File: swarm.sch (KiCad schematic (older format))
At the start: 24 parts, among them P1 USB_OTG, P2 CONN_02X20, P3 CONN_01X05, SW1 SW_PUSH, U1 STM32F103RETx, U2 LM3671MF-3.3, Y1 Crystal

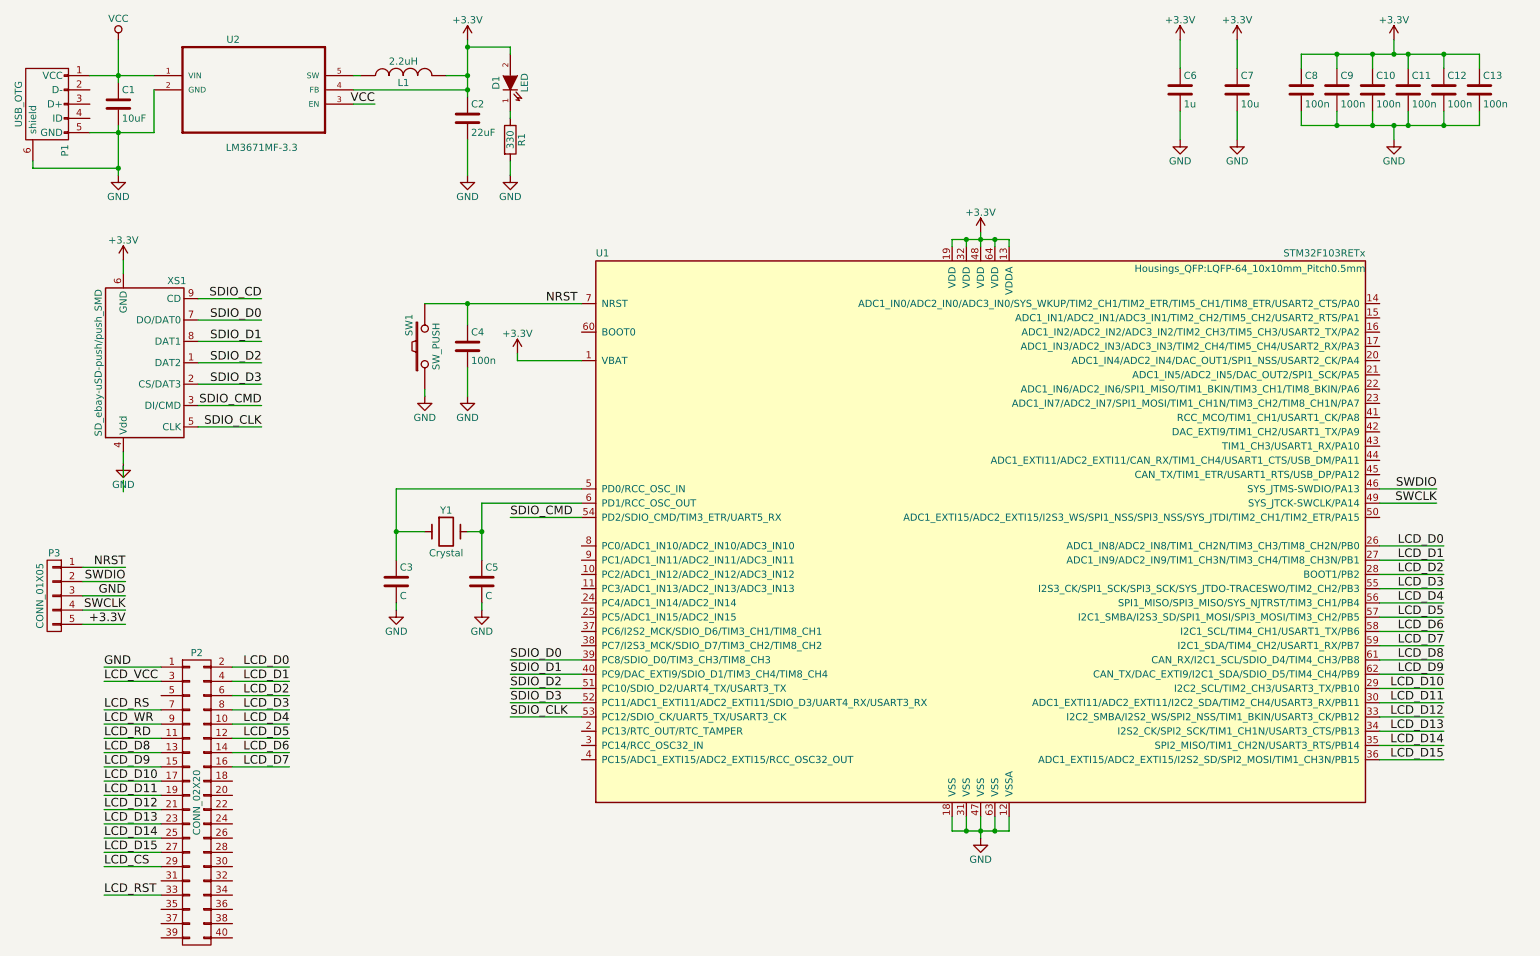
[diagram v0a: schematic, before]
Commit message: Adds APA102 SPI RGB LED Updates schematic references and links docoupling capacitors based on input pin
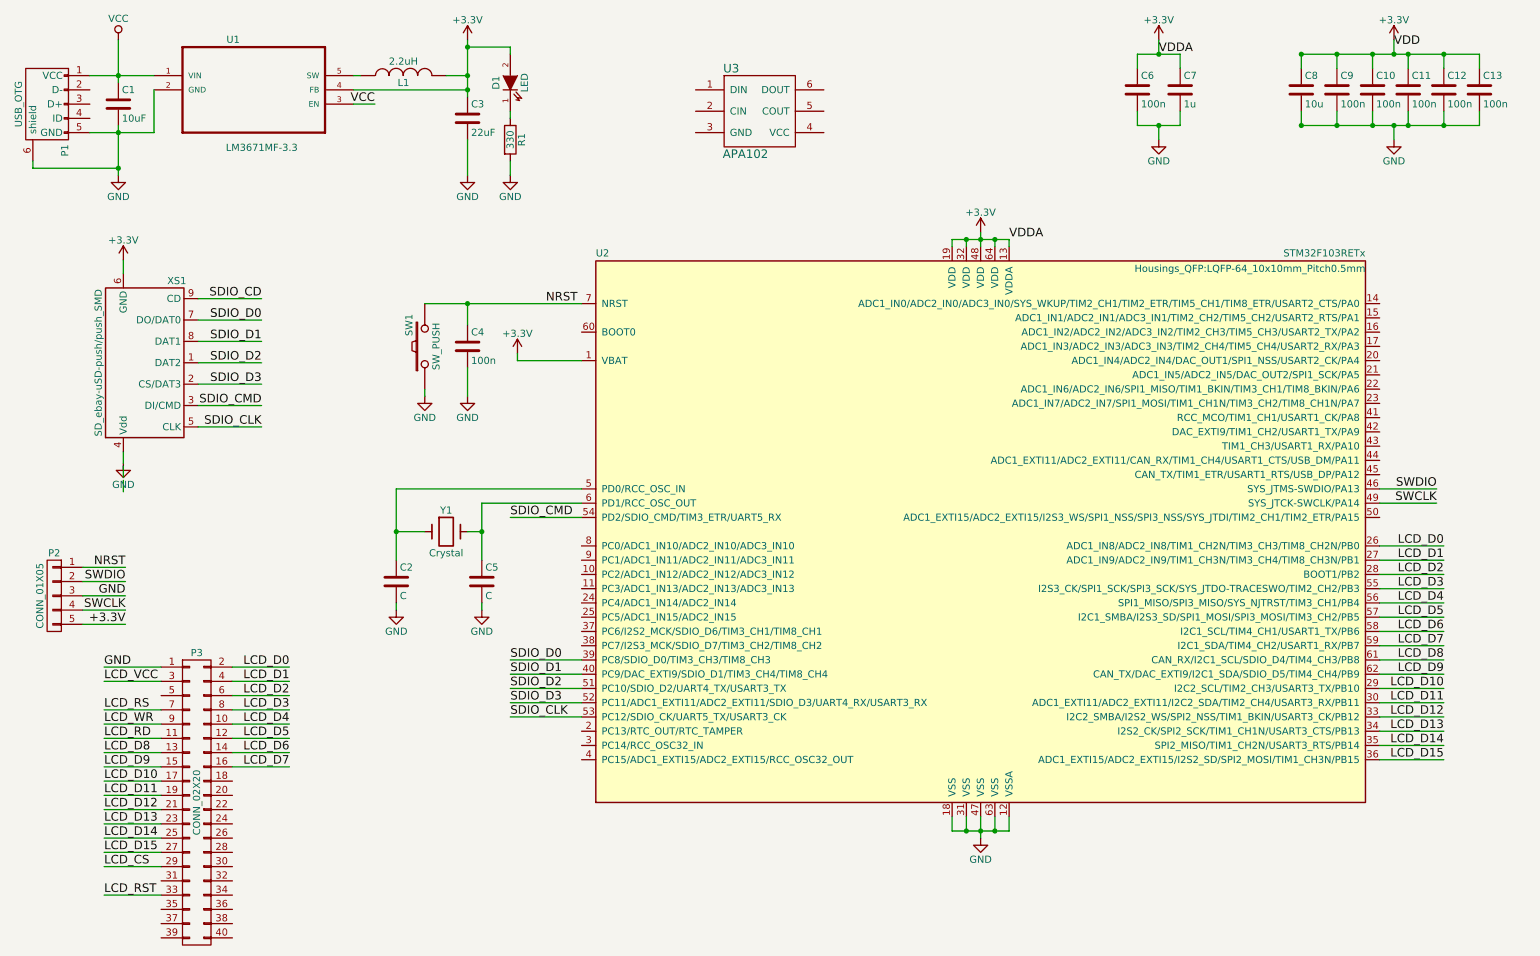
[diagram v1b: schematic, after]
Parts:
- added U3: APA102, volium:APA102, symbol APA102
- renumbered C3 to C2, C2 to C3, C8 to C6, C6 to C7, C7 to C8, P3 to P2, P2 to P3, U2 to U1, U1 to U2
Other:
- moved on the sheet: C6, C8
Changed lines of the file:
@@
 $EndDescr
 $Comp
-L +3.3V #PWR01
+L +3.3V #PWR13
 U 1 1 58134F73
 P 7450 2100
-F 0 "#PWR01" H 7450 1950 50  0001 C CNN
+F 0 "#PWR13" H 7450 1950 50  0001 C CNN
 F 1 "+3.3V" H 7450 2240 50  0000 C CNN
 F 2 "" H 7450 2100 50  0000 C CNN
@@
 $EndComp
 $Comp
-L GND #PWR02
+L GND #PWR14
 U 1 1 58134F89
 P 7450 6350
-F 0 "#PWR02" H 7450 6100 50  0001 C CNN
+F 0 "#PWR14" H 7450 6100 50  0001 C CNN
 F 1 "GND" H 7450 6200 50  0000 C CNN
 F 2 "" H 7450 6350 50  0000 C CNN
@@
 $EndComp
 $Comp
-L STM32F103RETx U1
+L STM32F103RETx U2
 U 1 1 581356E3
 P 7450 4200
-F 0 "U1" H 4750 6125 50  0000 L BNN
+F 0 "U2" H 4750 6125 50  0000 L BNN
 F 1 "STM32F103RETx" H 10150 6125 50  0000 R BNN
 F 2 "Housings_QFP:LQFP-64_10x10mm_Pitch0.5mm" H 10150 6075 50  0000 R TNN
@@
 $EndComp
 $Comp
-L +3.3V #PWR03
+L +3.3V #PWR12
 U 1 1 581369FC
 P 4200 2950
-F 0 "#PWR03" H 4200 2800 50  0001 C CNN
+F 0 "#PWR12" H 4200 2800 50  0001 C CNN
 F 1 "+3.3V" H 4200 3090 50  0000 C CNN
 F 2 "" H 4200 2950 50  0000 C CNN
@@
 $EndComp
 $Comp
-L C C8
+L C C6
 U 1 1 58136AF0
-P 9700 1100
-F 0 "C8" H 9725 1200 50  0000 L CNN
-F 1 "100n" H 9725 1000 50  0000 L CNN
-F 2 "Capacitors_SMD:C_1206" H 9738 950 50  0001 C CNN
-F 3 "" H 9700 1100 50  0000 C CNN
-	1    9700 1100
+P 8550 1100
+F 0 "C6" H 8575 1200 50  0000 L CNN
+F 1 "100n" H 8575 1000 50  0000 L CNN
+F 2 "Capacitors_SMD:C_1206" H 8588 950 50  0001 C CNN
+F 3 "" H 8550 1100 50  0000 C CNN
+	1    8550 1100
 	1    0    0    -1
 $EndComp
@@
 $EndComp
 $Comp
-L +3.3V #PWR04
+L +3.3V #PWR17
 U 1 1 58136B0C
 P 10350 750
-F 0 "#PWR04" H 10350 600 50  0001 C CNN
+F 0 "#PWR17" H 10350 600 50  0001 C CNN
 F 1 "+3.3V" H 10350 890 50  0000 C CNN
 F 2 "" H 10350 750 50  0000 C CNN
@@
 $EndComp
 $Comp
-L GND #PWR05
+L GND #PWR18
 U 1 1 58136D49
 P 10350 1450
-F 0 "#PWR05" H 10350 1200 50  0001 C CNN
+F 0 "#PWR18" H 10350 1200 50  0001 C CNN
 F 1 "GND" H 10350 1300 50  0000 C CNN
 F 2 "" H 10350 1450 50  0000 C CNN
@@
 $EndComp
 $Comp
+L C C8
+U 1 1 58137098
+P 9700 1100
+F 0 "C8" H 9725 1200 50  0000 L CNN
+F 1 "10u" H 9725 1000 50  0000 L CNN
+F 2 "Capacitors_SMD:C_1206" H 9738 950 50  0001 C CNN
+F 3 "" H 9700 1100 50  0000 C CNN
+	1    9700 1100
+	1    0    0    -1
+$EndComp
+$Comp
 L C C7
-U 1 1 58137098
-P 9250 1100
-F 0 "C7" H 9275 1200 50  0000 L CNN
-F 1 "10u" H 9275 1000 50  0000 L CNN
-F 2 "Capacitors_SMD:C_1206" H 9288 950 50  0001 C CNN
-F 3 "" H 9250 1100 50  0000 C CNN
-	1    9250 1100
-	1    0    0    -1
-$EndComp
-$Comp
-L +3.3V #PWR06
-U 1 1 581373B1
-P 9250 750
-F 0 "#PWR06" H 9250 600 50  0001 C CNN
-F 1 "+3.3V" H 9250 890 50  0000 C CNN
-F 2 "" H 9250 750 50  0000 C CNN
-F 3 "" H 9250 750 50  0000 C CNN
-	1    9250 750
-	1    0    0    -1
-$EndComp
-$Comp
-L GND #PWR07
-U 1 1 581375CE
-P 9250 1450
-F 0 "#PWR07" H 9250 1200 50  0001 C CNN
-F 1 "GND" H 9250 1300 50  0000 C CNN
-F 2 "" H 9250 1450 50  0000 C CNN
-F 3 "" H 9250 1450 50  0000 C CNN
-	1    9250 1450
-	1    0    0    -1
-$EndComp
-$Comp
-L C C6
 U 1 1 581377A0
 P 8850 1100
-F 0 "C6" H 8875 1200 50  0000 L CNN
+F 0 "C7" H 8875 1200 50  0000 L CNN
 F 1 "1u" H 8875 1000 50  0000 L CNN
 F 2 "Capacitors_SMD:C_1206" H 8888 950 50  0001 C CNN
@@
 $EndComp
 $Comp
-L +3.3V #PWR08
+L +3.3V #PWR15
 U 1 1 581377EE
-P 8850 750
-F 0 "#PWR08" H 8850 600 50  0001 C CNN
-F 1 "+3.3V" H 8850 890 50  0000 C CNN
-F 2 "" H 8850 750 50  0000 C CNN
-F 3 "" H 8850 750 50  0000 C CNN
-	1    8850 750
-	1    0    0    -1
-$EndComp
-$Comp
-L GND #PWR09
+P 8700 750
+F 0 "#PWR15" H 8700 600 50  0001 C CNN
+F 1 "+3.3V" H 8700 890 50  0000 C CNN
+F 2 "" H 8700 750 50  0000 C CNN
+F 3 "" H 8700 750 50  0000 C CNN
+	1    8700 750
+	1    0    0    -1
+$EndComp
+$Comp
+L GND #PWR16
 U 1 1 58137814
-P 8850 1450
-F 0 "#PWR09" H 8850 1200 50  0001 C CNN
-F 1 "GND" H 8850 1300 50  0000 C CNN
-F 2 "" H 8850 1450 50  0000 C CNN
-F 3 "" H 8850 1450 50  0000 C CNN
-	1    8850 1450
+P 8700 1450
+F 0 "#PWR16" H 8700 1200 50  0001 C CNN
+F 1 "GND" H 8700 1300 50  0000 C CNN
+F 2 "" H 8700 1450 50  0000 C CNN
+F 3 "" H 8700 1450 50  0000 C CNN
+	1    8700 1450
 	1    0    0    -1
 $EndComp
@@
 $EndComp
 $Comp
-L GND #PWR010
+L GND #PWR9
 U 1 1 581385B4
 P 3850 3250
-F 0 "#PWR010" H 3850 3000 50  0001 C CNN
+F 0 "#PWR9" H 3850 3000 50  0001 C CNN
 F 1 "GND" H 3850 3100 50  0000 C CNN
 F 2 "" H 3850 3250 50  0000 C CNN
@@
 $EndComp
 $Comp
-L GND #PWR011
+L GND #PWR6
 U 1 1 581389B8
 P 3550 3250
-F 0 "#PWR011" H 3550 3000 50  0001 C CNN
+F 0 "#PWR6" H 3550 3000 50  0001 C CNN
 F 1 "GND" H 3550 3100 50  0000 C CNN
 F 2 "" H 3550 3250 50  0000 C CNN
@@
 $EndComp
 $Comp
-L GND #PWR012
+L GND #PWR5
 U 1 1 581394F8
 P 3350 4750
-F 0 "#PWR012" H 3350 4500 50  0001 C CNN
+F 0 "#PWR5" H 3350 4500 50  0001 C CNN
 F 1 "GND" H 3350 4600 50  0000 C CNN
 F 2 "" H 3350 4750 50  0000 C CNN
@@
 $EndComp
 $Comp
-L C C3
+L C C2
 U 1 1 5813962D
 P 3350 4550
-F 0 "C3" H 3375 4650 50  0000 L CNN
+F 0 "C2" H 3375 4650 50  0000 L CNN
 F 1 "C" H 3375 4450 50  0000 L CNN
 F 2 "Capacitors_SMD:C_1206" H 3388 4400 50  0001 C CNN
@@
 $EndComp
 $Comp
-L GND #PWR013
+L GND #PWR10
 U 1 1 581398A2
 P 3950 4750
-F 0 "#PWR013" H 3950 4500 50  0001 C CNN
+F 0 "#PWR10" H 3950 4500 50  0001 C CNN
 F 1 "GND" H 3950 4600 50  0000 C CNN
 F 2 "" H 3950 4750 50  0000 C CNN
@@
 $EndComp
 $Comp
-L LM3671MF-3.3 U2
+L LM3671MF-3.3 U1
 U 1 1 5840B3E1
 P 2350 1000
-F 0 "U2" H 2158 1253 50  0000 L CNN
+F 0 "U1" H 2158 1253 50  0000 L CNN
 F 1 "LM3671MF-3.3" H 2154 495 50  0000 L CNN
 F 2 "TO_SOT_Packages_SMD:SOT-23-5" H 2350 1000 50  0001 L CNN
@@
 $EndComp
 $Comp
-L C C2
+L C C3
 U 1 1 5840B3E4
 P 3850 1300
-F 0 "C2" H 3875 1400 50  0000 L CNN
+F 0 "C3" H 3875 1400 50  0000 L CNN
 F 1 "22uF" H 3875 1200 50  0000 L CNN
 F 2 "Capacitors_SMD:C_1206" H 3888 1150 50  0001 C CNN
@@
 $EndComp
 $Comp
-L +3.3V #PWR014
+L +3.3V #PWR7
 U 1 1 5840B3E6
 P 3850 750
-F 0 "#PWR014" H 3850 600 50  0001 C CNN
+F 0 "#PWR7" H 3850 600 50  0001 C CNN
 F 1 "+3.3V" H 3850 890 50  0000 C CNN
 F 2 "" H 3850 750 50  0000 C CNN
@@
 $EndComp
 $Comp
-L VCC #PWR015
+L VCC #PWR1
 U 1 1 5840B3E8
 P 1400 750
-F 0 "#PWR015" H 1400 600 50  0001 C CNN
+F 0 "#PWR1" H 1400 600 50  0001 C CNN
 F 1 "VCC" H 1400 900 50  0000 C CNN
 F 2 "" H 1400 750 50  0000 C CNN
@@
 $EndComp
 $Comp
-L GND #PWR016
+L GND #PWR8
 U 1 1 5840B3E9
 P 3850 1700
-F 0 "#PWR016" H 3850 1450 50  0001 C CNN
+F 0 "#PWR8" H 3850 1450 50  0001 C CNN
 F 1 "GND" H 3850 1550 50  0000 C CNN
 F 2 "" H 3850 1700 50  0000 C CNN
@@
 $EndComp
 $Comp
-L GND #PWR017
+L GND #PWR2
 U 1 1 5840B3EA
 P 1400 1700
-F 0 "#PWR017" H 1400 1450 50  0001 C CNN
+F 0 "#PWR2" H 1400 1450 50  0001 C CNN
 F 1 "GND" H 1400 1550 50  0000 C CNN
 F 2 "" H 1400 1700 50  0000 C CNN
@@
 $EndComp
 $Comp
-L GND #PWR018
+L GND #PWR11
 U 1 1 5840B3ED
 P 4150 1700
-F 0 "#PWR018" H 4150 1450 50  0001 C CNN
+F 0 "#PWR11" H 4150 1450 50  0001 C CNN
 F 1 "GND" H 4150 1550 50  0000 C CNN
 F 2 "" H 4150 1700 50  0000 C CNN
@@
 	4200 3000 4200 2950
 Wire Wire Line
-	9700 950  9700 850
-Wire Wire Line
-	9700 850  10950 850
-Wire Wire Line
 	10950 850  10950 950
 Wire Wire Line
-	10700 950  10700 850
+	10700 850  10700 950
 Connection ~ 10700 850
 Wire Wire Line
-	10450 950  10450 850
+	10450 850  10450 950
 Connection ~ 10450 850
 Wire Wire Line
-	10200 950  10200 850
+	10200 850  10200 950
 Connection ~ 10200 850
 Wire Wire Line
 	9950 950  9950 850
-Connection ~ 9950 850
-Wire Wire Line
-	10350 750  10350 850
+Wire Wire Line
+	10350 850  10350 750
 Connection ~ 10350 850
-Wire Wire Line
-	9700 1250 9700 1350
 Wire Wire Line
 	9700 1350 10950 1350
@@
 Wire Wire Line
 	9950 1250 9950 1350
-Connection ~ 9950 1350
 Wire Wire Line
 	10350 1450 10350 1350
 Connection ~ 10350 1350
 Wire Wire Line
-	9250 950  9250 750
-Wire Wire Line
-	9250 1450 9250 1250
-Wire Wire Line
-	8850 1450 8850 1250
-Wire Wire Line
-	8850 950  8850 750
+	9700 950  9700 850
+Wire Wire Line
+	9700 1350 9700 1250
+Wire Wire Line
+	8700 1350 8700 1450
 Wire Wire Line
 	3850 3050 3850 3250
@@
 SDIO_CD
 $Comp
-L +3.3V #PWR019
+L +3.3V #PWR3
 U 1 1 58424C6C
 P 1435 2295
-F 0 "#PWR019" H 1435 2145 50  0001 C CNN
+F 0 "#PWR3" H 1435 2145 50  0001 C CNN
 F 1 "+3.3V" H 1435 2435 50  0000 C CNN
 F 2 "" H 1435 2295 50  0000 C CNN
@@
 	1435 2295 1435 2390
 $Comp
-L GND #PWR020
+L GND #PWR4
 U 1 1 5842512A
 P 1435 3720
-F 0 "#PWR020" H 1435 3470 50  0001 C CNN
+F 0 "#PWR4" H 1435 3470 50  0001 C CNN
 F 1 "GND" H 1435 3570 50  0000 C CNN
 F 2 "" H 1435 3720 50  0000 C CNN
@@
 	1435 3920 1435 3840
 $Comp
-L CONN_02X20 P2
+L CONN_02X20 P3
 U 1 1 58432580
 P 1950 6100
-F 0 "P2" H 1950 7150 50  0000 C CNN
+F 0 "P3" H 1950 7150 50  0000 C CNN
 F 1 "CONN_02X20" V 1950 6100 50  0000 C CNN
 F 2 "Pin_Headers:Pin_Header_Straight_2x20" H 1950 5150 50  0001 C CNN
@@
 LCD_RST
 $Comp
-L CONN_01X05 P3
+L CONN_01X05 P2
 U 1 1 584388C3
 P 950 4650
-F 0 "P3" H 950 4950 50  0000 C CNN
+F 0 "P2" H 950 4950 50  0000 C CNN
 F 1 "CONN_01X05" V 1050 4650 50  0000 C CNN
 F 2 "Pin_Headers:Pin_Header_Angled_1x05" H 950 4650 50  0001 C CNN
@@
 Text Label 10650 3900 2    60   ~ 0
 SWDIO
+Text Label 7650 2150 0    60   ~ 0
+VDDA
+Text Label 8700 850  0    60   ~ 0
+VDDA
+Wire Wire Line
+	9700 850  10950 850
+Wire Wire Line
+	8550 950  8550 850
+Connection ~ 9950 1350
+Connection ~ 9700 1350
+Connection ~ 9700 850
+Connection ~ 9950 850
+Wire Wire Line
+	8550 1250 8550 1350
+Wire Wire Line
+	8550 1350 8850 1350
+Wire Wire Line
+	8850 1350 8850 1250
+Connection ~ 8700 1350
+Wire Wire Line
+	8850 850  8850 950
+Wire Wire Line
+	8550 850  8850 850
+Wire Wire Line
+	8700 850  8700 750
+Connection ~ 8700 850
+Text Label 10350 800  0    60   ~ 0
+VDD
+$Comp
+L APA102 U3
+U 1 1 58445D7D
+P 5900 1250
+F 0 "U3" H 5700 1550 60  0000 C CNN
+F 1 "APA102" H 5800 950 60  0000 C CNN
+F 2 "volium:APA102" H 5900 800 60  0001 C CNN
+F 3 "" H 5900 800 60  0000 C CNN
+	1    5900 1250
+	1    0    0    -1
+$EndComp
 $EndSCHEMATC

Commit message: Moves some components around, no significant changes
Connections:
- net GND: now also U3.3 (GND)
- net VCC: now also U3.4 (VCC)
- net RGB_LED_CIN: now reaches U2.21 (ADC1_IN5/ADC2_IN5/DAC_OUT2/SPI1_SCK/PA5)
- net RGB_LED_CIN: now also U3.2 (CIN)
- net RGB_LED_DIN: now reaches U2.23 (ADC1_IN7/ADC2_IN7/SPI1_MOSI/TIM1_CH1N/TIM3_CH2/TIM8_CH1N/PA7)
- net RGB_LED_DIN: now also U3.1 (DIN)
